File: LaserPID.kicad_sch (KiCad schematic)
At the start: 55 parts, among them P1 POWER, P2 IN1, P3 IN2, P4 Out, P5 RST, U1 INA105, U2 LM741, U3 LM741, U4 LM741, U6 LM741, U7 DG419

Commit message: Some updates to part list for no-longer-available parts
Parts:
- C1, C2, C3: Digikey Part Number 493-1355-ND -> 493-17046-ND
- P2, P3, P4, P5: Digikey Part Number A97553-ND -> ARF1690-ND
- U1: Digikey Part Number INA105KP-ND -> AMP03GPZ-ND
- U7: Digikey Part Number DG419LDY+TCT-ND -> DG469EY-T1-E3CT-ND
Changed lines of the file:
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@@
     )
     (property "Datasheet" "" (id 3) (at 33.02 119.38 0))
-    (property "Digikey Part Number" "A97553-ND" (id 4) (at 33.02 119.38 0)
+    (property "Digikey Part Number" "ARF1690-ND" (id 4) (at 33.02 119.38 0)
       (effects (font (size 1.27 1.27)) hide)
     )
@@
     )
     (property "Datasheet" "" (id 3) (at 33.02 133.35 0))
-    (property "Digikey Part Number" "A97553-ND" (id 4) (at 33.02 133.35 0)
+    (property "Digikey Part Number" "ARF1690-ND" (id 4) (at 33.02 133.35 0)
       (effects (font (size 1.27 1.27)) hide)
     )
@@
     )
     (property "Datasheet" "" (id 3) (at 250.19 125.73 0))
-    (property "Digikey Part Number" "A97553-ND" (id 4) (at 250.19 125.73 0)
+    (property "Digikey Part Number" "ARF1690-ND" (id 4) (at 250.19 125.73 0)
       (effects (font (size 1.27 1.27)) hide)
     )
@@
     )
     (property "Datasheet" "" (id 3) (at 83.82 132.08 0))
-    (property "Digikey Part Number" "INA105KP-ND" (id 4) (at 80.01 128.27 0)
+    (property "Digikey Part Number" "AMP03GPZ-ND" (id 4) (at 80.01 128.27 0)
       (effects (font (size 1.27 1.27)) hide)
     )
@@
     )
     (property "Datasheet" "" (id 3) (at 66.04 43.18 0))
-    (property "Digikey Part Number" "493-1355-ND " (id 4) (at 66.04 43.18 0)
+    (property "Digikey Part Number" "493-17046-ND" (id 4) (at 66.04 43.18 0)
       (effects (font (size 1.27 1.27)) hide)
     )
@@
     )
     (property "Datasheet" "" (id 3) (at 58.42 39.37 0))
-    (property "Digikey Part Number" "493-1355-ND " (id 4) (at 58.42 39.37 0)
+    (property "Digikey Part Number" "493-17046-ND" (id 4) (at 58.42 39.37 0)
       (effects (font (size 1.27 1.27)) hide)
     )
@@
     )
     (property "Datasheet" "" (id 3) (at 58.42 46.99 0))
-    (property "Digikey Part Number" "493-1355-ND " (id 4) (at 58.42 46.99 0)
+    (property "Digikey Part Number" "493-17046-ND" (id 4) (at 58.42 46.99 0)
       (effects (font (size 1.27 1.27)) hide)
     )
@@
     )
     (property "Datasheet" "" (id 3) (at 34.29 81.28 0))
-    (property "Digikey Part Number" "A97553-ND" (id 4) (at 34.29 81.28 0)
+    (property "Digikey Part Number" "ARF1690-ND" (id 4) (at 34.29 81.28 0)
       (effects (font (size 1.27 1.27)) hide)
     )
@@
       (effects (font (size 1.524 1.524)))
     )
-    (property "Digikey Part Number" "DG419LDY+TCT-ND" (id 4) (at 114.3 52.07 0)
-      (effects (font (size 1.27 1.27)) hide)
-    )
+    (property "Digikey Part Number" "DG469EY-T1-E3CT-ND" (id 4) (at 114.3 52.07 0)
+      (effects (font (size 1.27 1.27)) hide)
+    )

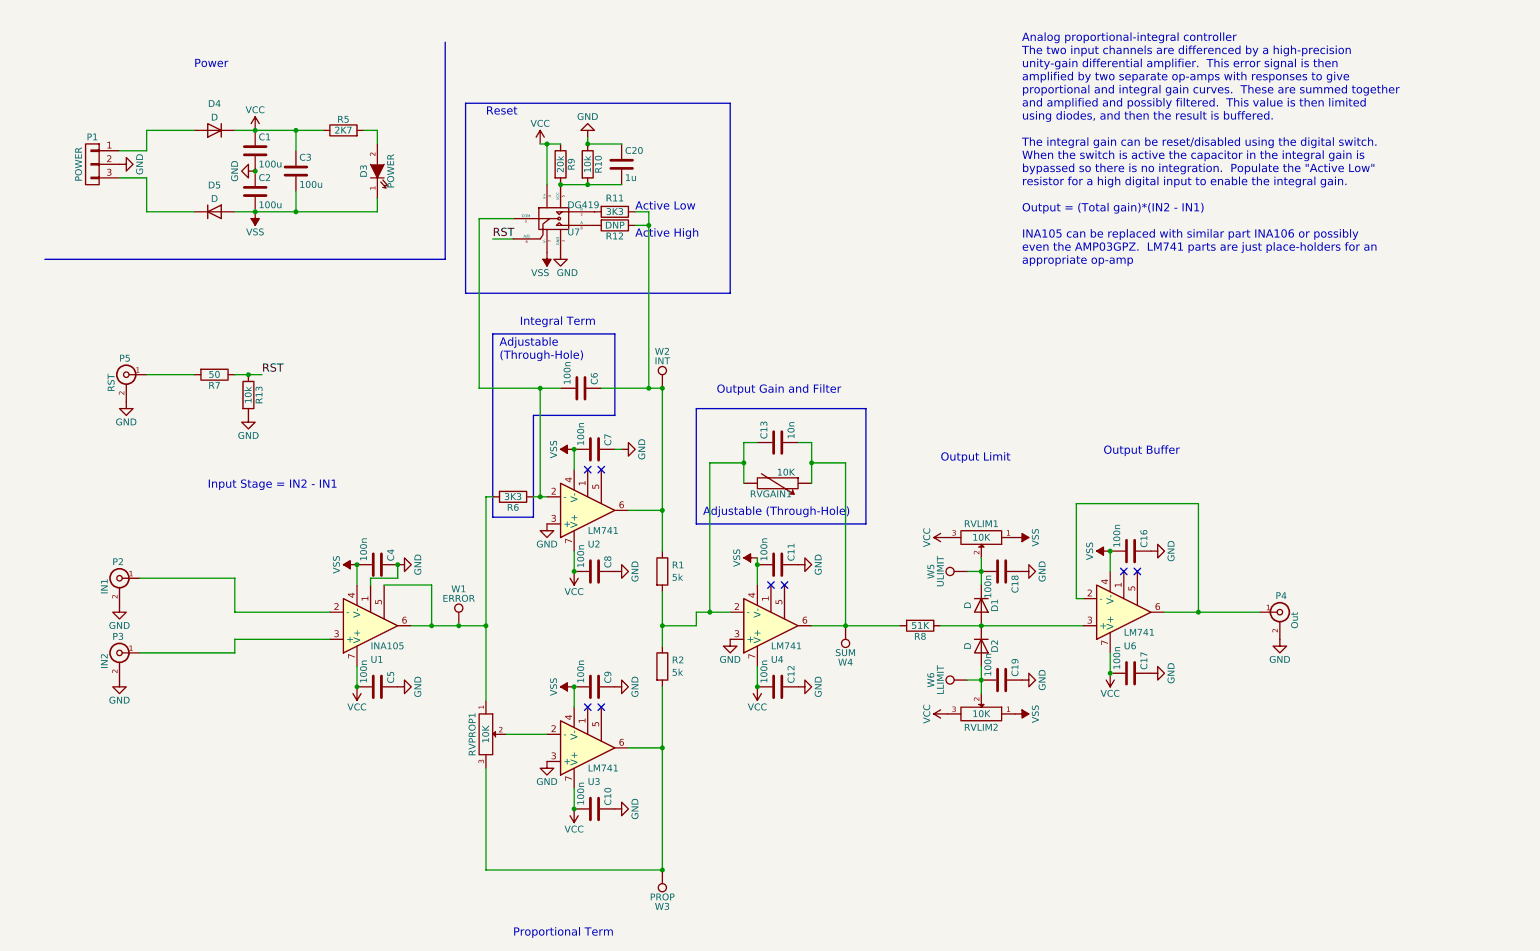
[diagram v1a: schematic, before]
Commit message: Update to board with over- and reverse-voltage protection.
Smaller board as well to fit in boxes from Digikey.  All BNCs on
the same side, power on opposite side.  Switch included to go between
open and closed loop control
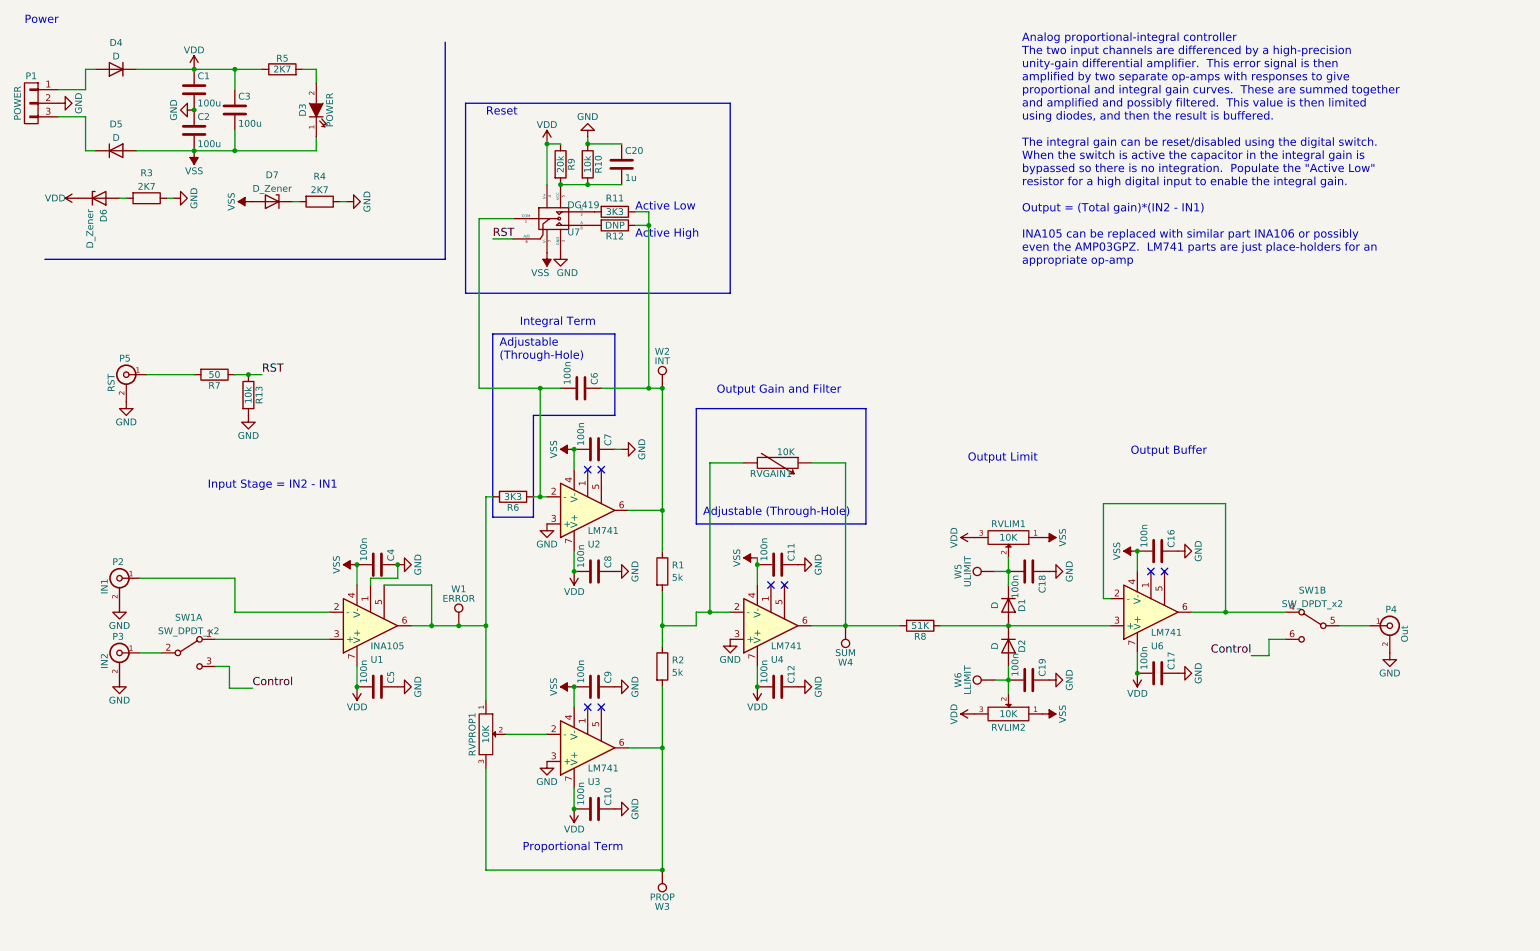
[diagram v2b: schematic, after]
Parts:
- removed C13: 10n, pi-servo-board:R_Universal_L13.0mm_W4.0mm_P9.00mm, symbol Device:C
- added D6, D7: D_Zener, pi-servo-board:DIODE-SOD-123, symbol Device:D_Zener
- added R3, R4: 2K7, Resistor_SMD:R_1206_3216Metric_Pad1.30x1.75mm_HandSolder, symbol Device:R
- added SW1: SW_DPDT_x2, pi-servo-board:DPDT_SW_ADAM_TECH, symbol Switch:SW_DPDT_x2
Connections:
- net GND: now also R3.1, R4.1
- net VSS: now also D7.2 (A)
- net at P3.1 (In): now also SW1.2 (B); no longer U1.3 (+)
- net at U6.2 (-), U6.6: now also SW1.4 (A); no longer P4.1 (In)
- net VCC renamed VDD
- net VDD: now also D6.1 (K)
- new net: P4.1 (In), SW1.5 (B)
- new net: SW1.1 (A), U1.3 (+)
- new net: D7.1 (K), R4.2
- new net: D6.2 (A), R3.2
- new net Control: SW1.3 (C), SW1.6 (C)
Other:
- moved on the sheet: C1, C16, C17, C18, C19, C2, C3, D1, D2, D3, D4, D5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

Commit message: Updated board, sent for production
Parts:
- removed D6, D7: D_Zener, pi-servo-board:DIODE-SOD-123, symbol Device:D_Zener
- removed R3, R4: 2K7, Resistor_SMD:R_1206_3216Metric_Pad1.30x1.75mm_HandSolder, symbol Device:R
- added C13: 100n, Capacitor_SMD:C_1206_3216Metric_Pad1.33x1.80mm_HandSolder, symbol Device:C
- added U5: MC78L12_TO92, Package_TO_SOT_THT:TO-92_Inline, symbol Regulator_Linear:MC78L12_TO92
- added U8: MC79L12_TO92, Package_TO_SOT_THT:TO-92_Inline, symbol pi-servo-board:MC79L12_TO92
- C1, C2: value 100u -> 330n; footprint Capacitor_THT:CP_Radial_D10.0mm_P5.00mm -> Capacitor_SMD:C_1206_3216Metric_Pad1.33x1.80mm_HandSolder; Digikey Part Number 493-17046-ND -> 4713-GMC31X7R334K50NTCT-ND
- C3: value 100u -> 100n; footprint Capacitor_THT:CP_Radial_D10.0mm_P5.00mm -> Capacitor_SMD:C_1206_3216Metric_Pad1.33x1.80mm_HandSolder; Digikey Part Number 493-17046-ND -> 478-1556-1-ND
- U2, U3, U4, U6: Digikey Part Number OP07DNZ-ND -> 296-34251-5-ND
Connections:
- net GND: now also C3.2, C13.1, U5.2 (GND), U8.1 (GND)
- net VDD: now also R5.2, U5.1 (VO); no longer C1.1, D4.1 (K), R5.1
- net VSS: now also C13.2, U8.3 (VO); no longer C2.2, C3.2, D5.2 (A)
- net at D3.2 (A): now also R5.1; no longer R5.2
- new net: C2.2, D5.2 (A), U8.2 (VI)
- new net: C1.1, D4.1 (K), U5.3 (VI)
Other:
- moved on the sheet: D3, D4, D5, P1, R5
